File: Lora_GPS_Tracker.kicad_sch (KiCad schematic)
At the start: 19 parts, among them J1 USB_C_Receptacle_USB2.0_16P, U1 STM32G031G6Ux, U2 E220-900T22S, U3 USBLC6-2SC6, U4 TPS631000DRLR, U5 MCP73831-2-OT

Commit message: feat: finish gps & lora sch design
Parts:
- added AE1: Antenna, symbol Device:Antenna
- added C10, C11, C14, C15: 100n, symbol Device:C
- added C12, C13: 10u, symbol Device:C
- added C16: 100p, symbol Device:C
- added C2: C_Polarized, symbol Device:C_Polarized
- added J2: Conn_Coaxial, symbol Connector:Conn_Coaxial
- added L2: 33n, symbol Device:L
- added R10: 10R, symbol Device:R
- added R7: 0R, symbol Device:R
- added R8, R9: 10k, symbol Device:R
- added U6: GP-02, symbol GP-02:GP-02
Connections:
- net +3V3: now also U2.10 (VCC), C10.1, C12.1, C13.1, C14.1, U6.8 (VCC)
- net GND: now also C10.2, C11.2, C12.2, C13.2, C14.2, C15.2, C2.2, J2.2 (Ext), R7.2, R8.2, R9.2, U6.1 (GND), U6.10 (GND), U6.12 (GND)
- net at U2.21 (ANT): now also J2.1 (In)
- net M0: now reaches U2.5 (M0)
- net M0: now also R9.1
- net M1: now reaches U2.6 (M1)
- net M1: now also R8.1
- net LORA_TX: now reaches U2.7 (RXD)
- net LORA_RX: now reaches U2.8 (TXD)
- net AUX: now reaches U2.9 (AUX)
- new net: C11.1, C2.1, U6.6 (VRTC)
- new net: R7.1, U6.13 (IO8)
- new net: C16.1, U6.11 (RF_IN)
- new net: R10.1, U6.14 (VCC_RF)
- new net: AE1.1 (A), C16.2, L2.1
- new net: C15.1, L2.2, R10.2
- new net GPS_RX: U6.2 (TXD)
- new net GPS_TX: U6.3 (RXD)
- new net N/F: U6.5 (ON/OFF)
- new net PPS: U6.4 (PPS)
- no-connect marks 2 -> 7
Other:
- moved on the sheet: U2

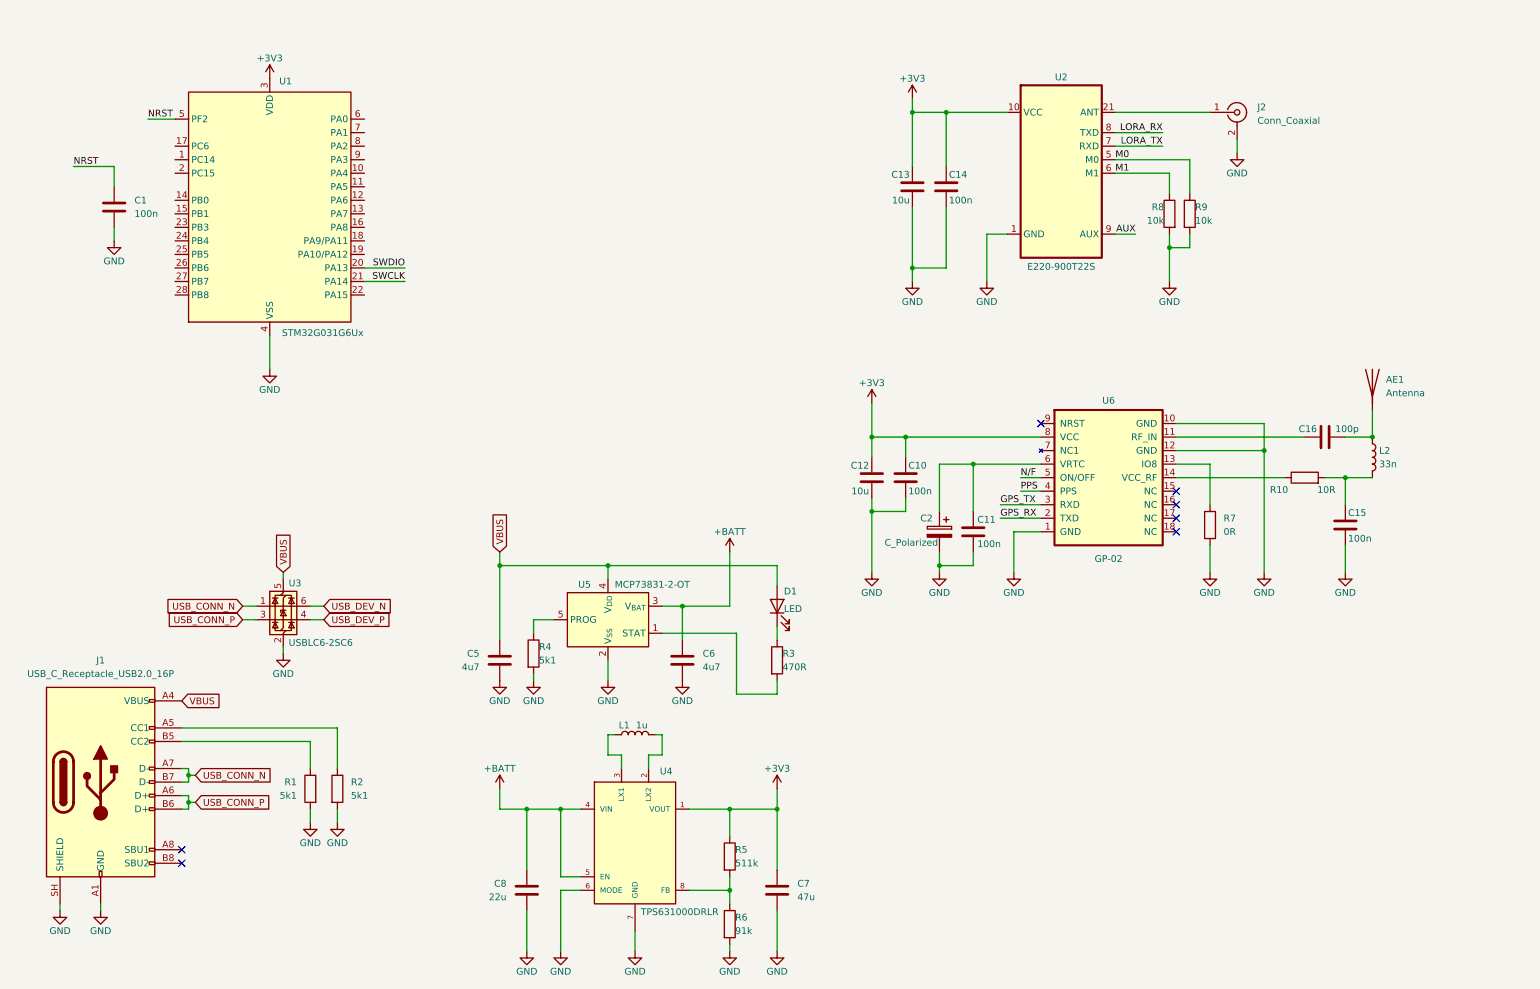
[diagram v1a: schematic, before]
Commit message: feat: finish battery & swd pins; need to assign mcu pinout
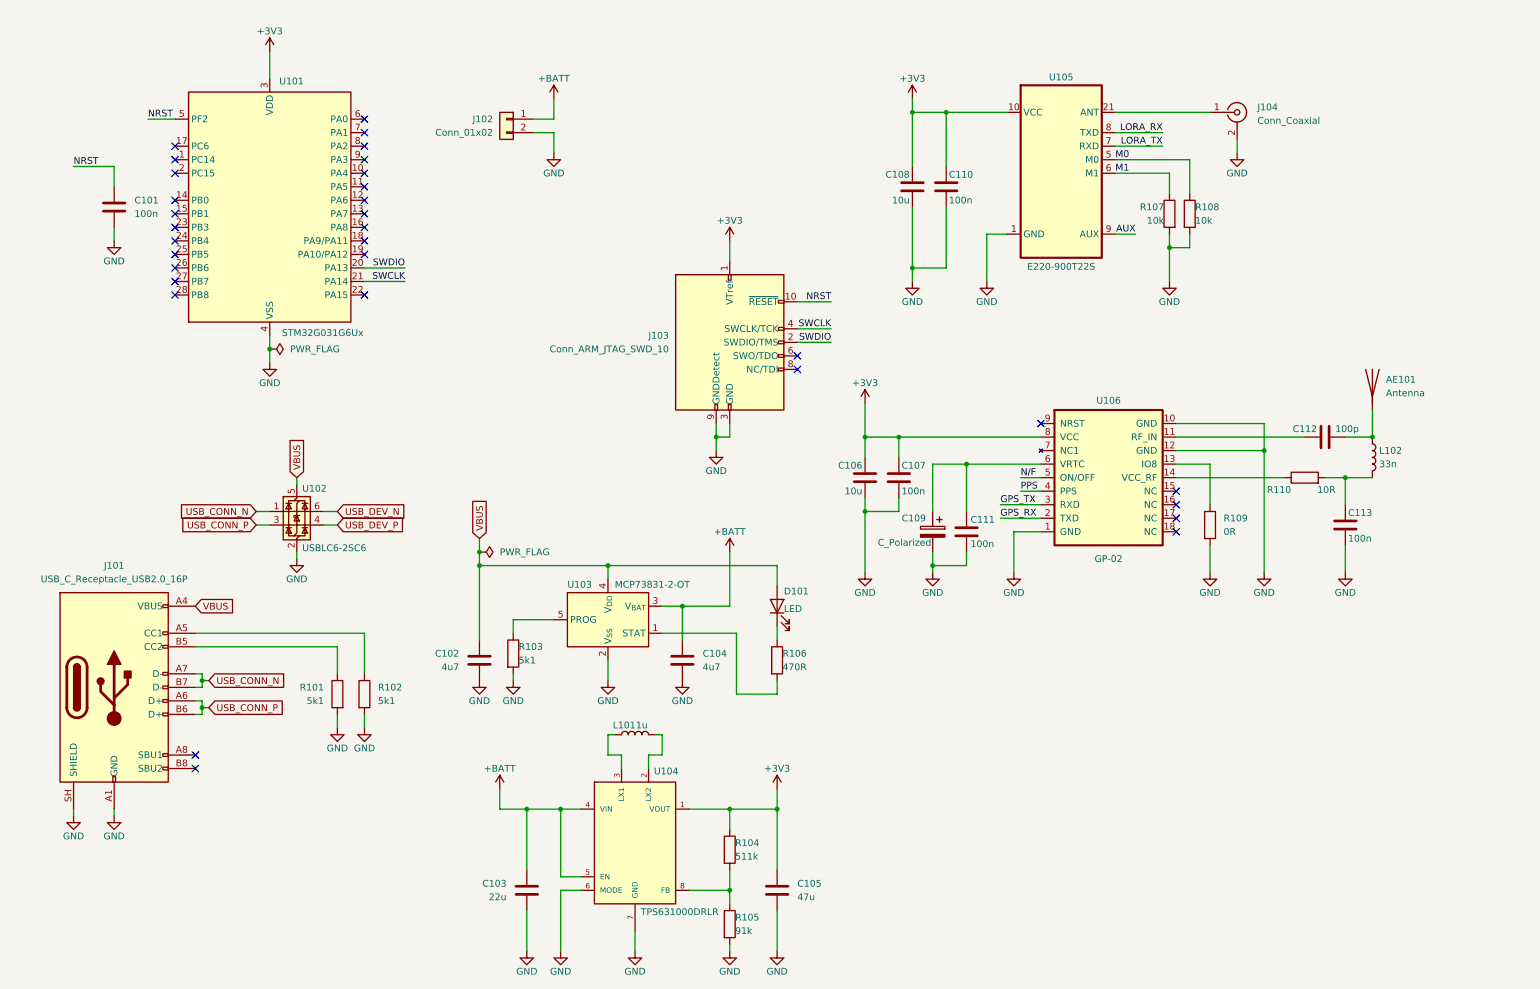
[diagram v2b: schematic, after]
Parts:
- added J102: Conn_01x02, symbol Connector_Generic:Conn_01x02
- added J103: Conn_ARM_JTAG_SWD_10, symbol Connector:Conn_ARM_JTAG_SWD_10
- renumbered AE1 to AE101, C1 to C101, C5 to C102, C8 to C103, C6 to C104, C7 to C105, C12 to C106, C10 to C107, C13 to C108, C2 to C109, C14 to C110, C11 to C111, C16 to C112, C15 to C113, D1 to D101, J1 to J101, J2 to J104, L1 to L101, L2 to L102, R1 to R101, R2 to R102, R4 to R103, R5 to R104, R6 to R105, R3 to R106, R8 to R107, R9 to R108, R7 to R109, R10 to R110, U1 to U101, U3 to U102, U5 to U103, U4 to U104, U2 to U105, U6 to U106
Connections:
- net +3V3: now also J103.1 (VTref)
- net +BATT: now also J102.1 (Pin_1)
- net GND: now also J102.2 (Pin_2), J103.3 (GND), J103.5 (GND), J103.9 (GNDDetect)
- net NRST: now also J103.10 (~{RESET})
- net SWCLK: now also J103.4 (SWCLK/TCK)
- net SWDIO: now also J103.2 (SWDIO/TMS)
- no-connect marks 7 -> 32
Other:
- moved on the sheet: C102, C106, C107, C109, C111, J101, R101, R102, R103, R104, U102

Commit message: feat: finish sch design
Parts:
- removed U102: USBLC6-2SC6, Package_TO_SOT_SMD:SOT-23-6, symbol Power_Protection:USBLC6-2SC6
- C101, C107, C110, C111, C112, C113: footprint (none) -> Capacitor_SMD:C_0402_1005Metric
- C102, C104, C106, C108: footprint (none) -> Capacitor_SMD:C_0603_1608Metric
- C103, C105: footprint (none) -> Capacitor_SMD:C_0805_2012Metric
- D101: footprint (none) -> LED_SMD:LED_0603_1608Metric
- L101, L102: footprint (none) -> Inductor_SMD:L_0603_1608Metric
- R101, R102, R103, R104, R105, R106, R107, R108, R109, R110: footprint (none) -> Resistor_SMD:R_0603_1608Metric
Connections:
- net AUX: now also U101.12 (PA6)
- net GPS_RX: now also U101.9 (PA3)
- net GPS_TX: now also U101.8 (PA2)
- net LORA_RX: now also U101.27 (PB7)
- net LORA_TX: now also U101.26 (PB6)
- net M0: now also U101.10 (PA4)
- net M1: now also U101.11 (PA5)
- net PPS: now also U101.13 (PA7)
- net N/F: no longer names the net of U106.5 (ON/OFF)
- net USB_CONN_N: no longer names the net of J101.A7 (D-)
- net USB_CONN_N: no longer J101.B7 (D-)
- net USB_CONN_P: no longer names the net of J101.A6 (D+)
- net USB_CONN_P: no longer J101.B6 (D+)
- no-connect marks 32 -> 29
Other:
- moved on the sheet: C101, C108, C109, C110, J101, J103, J104, R101, R102, R107, R108, U105

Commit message: feat: finish rough layout
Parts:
- removed AE101: Antenna, symbol Device:Antenna
- removed J103: Conn_ARM_JTAG_SWD_10, symbol Connector:Conn_ARM_JTAG_SWD_10
- added C102: 10u, Capacitor_SMD:C_0603_1608Metric, symbol Device:C
- added C103: 100n, Capacitor_SMD:C_0402_1005Metric, symbol Device:C
- added H101, H102, H103: MountingHole, MountingHole:MountingHole_2.2mm_M2, symbol Mechanical:MountingHole
- added J103: Conn_01x05_Pin, Connector_PinHeader_2.54mm:PinHeader_1x05_P2.54mm_Vertical, symbol Connector:Conn_01x05_Pin
- added J104, J105: Conn_01x02, Connector_PinHeader_2.54mm:PinHeader_1x02_P2.54mm_Vertical, symbol Connector_Generic:Conn_01x02
- added J107: Conn_Coaxial, Projects:ANT-SMD_KH-IPEX-K501-29, symbol Connector:Conn_Coaxial
- C110: renamed from C109; footprint (none) -> Projects:CAP-SMD_2P-L4.8-W4.8-TR
- J101: footprint (none) -> Connector_USB:USB_C_Receptacle_GCT_USB4105-xx-A_16P_TopMnt_Horizontal
- J102: footprint (none) -> Connector_JST:JST_PH_S2B-PH-K_1x02_P2.00mm_Horizontal
- J106: renamed from J104; footprint (none) -> Connector_Coaxial:SMA_Samtec_SMA-J-P-H-ST-EM1_EdgeMount
- U103: renamed from U104; footprint TPS631000DRLR:SOT50P160X60-8N -> Projects:TPS631000DRLR
- U104: renamed from U106; footprint (none) -> Projects:GP-02_FULL_PAD
- U105: footprint Project:WIRELM-SMD_E220-900T22S -> Projects:WIRELM-SMD_E220-900T22S
- renumbered C102 to C104, C103 to C105, C104 to C106, C105 to C107, C106 to C108, C107 to C109, C108 to C112, C110 to C113, C112 to C114, C113 to C115, R109 to R107, R107 to R108, R108 to R109, U103 to U102
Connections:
- net +3V3: now also C102.1, C103.1, J103.1 (Pin_1)
- net GND: now also C102.2, C103.2, J103.5 (Pin_5), J107.2 (Ext)
- net GPS_RX: now also J105.2 (Pin_2)
- net GPS_TX: now also J105.1 (Pin_1)
- net LORA_RX: now also J104.1 (Pin_1)
- net LORA_TX: now also J104.2 (Pin_2)
- net M0: now also U101.11 (PA5); no longer U101.10 (PA4)
- net M1: now also U101.10 (PA4); no longer U101.11 (PA5)
- net NRST: now also J103.2 (Pin_2)
- net SWCLK: now also J103.3 (Pin_3)
- net SWDIO: now also J103.4 (Pin_4)
- net at C114.2, L102.1: now also J107.1 (In)
- no-connect marks 29 -> 27
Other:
- moved on the sheet: C110, J102

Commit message: feat: finish baisc layout
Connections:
- net AUX: now also U101.11 (PA5); no longer U101.12 (PA6)
- net M0: now also U101.12 (PA6); no longer U101.11 (PA5)
- net SWCLK: now also J103.4 (Pin_4); no longer J103.3 (Pin_3)
- net SWDIO: now also J103.3 (Pin_3); no longer J103.4 (Pin_4)
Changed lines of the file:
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@@
 	(wire
 		(pts
-			(xy 137.16 60.96) (xy 143.51 60.96)
+			(xy 137.16 58.42) (xy 143.51 58.42)
 		)
 		(stroke
@@
 	(wire
 		(pts
-			(xy 80.01 46.99) (xy 87.63 46.99)
+			(xy 80.01 49.53) (xy 87.63 49.53)
 		)
 		(stroke
@@
 	(wire
 		(pts
-			(xy 80.01 49.53) (xy 87.63 49.53)
+			(xy 80.01 46.99) (xy 87.63 46.99)
 		)
 		(stroke
@@
 	(wire
 		(pts
-			(xy 137.16 58.42) (xy 143.51 58.42)
+			(xy 137.16 60.96) (xy 143.51 60.96)
 		)
 		(stroke
@@
 	)
 	(label "SWDIO"
-		(at 143.51 60.96 180)
+		(at 143.51 58.42 180)
 		(effects
 			(font
@@
 	)
 	(label "AUX"
-		(at 87.63 49.53 180)
+		(at 87.63 46.99 180)
 		(effects
 			(font
@@
 	)
 	(label "SWCLK"
-		(at 143.51 58.42 180)
+		(at 143.51 60.96 180)
 		(effects
 			(font
@@
 	)
 	(label "M0"
-		(at 87.63 46.99 180)
+		(at 87.63 49.53 180)
 		(effects
 			(font
